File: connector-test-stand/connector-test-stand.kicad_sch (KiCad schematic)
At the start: 85 parts, among them J1 Conn_01x02, J10 Conn_01x04_MountingPin, J11 DE9_Socket_MountingHoles, J12 DVI-I_Dual_Link, J2 Conn_01x02, J3 Conn_01x02, J4 Conn_01x05, J5 Conn_01x04_MountingPin, J6 Conn_01x02, J7 Conn_01x03, J8 Conn_01x10, J9 Conn_01x04_MountingPin, K1 G2RL-1-E, U1 PCF8574RGTR, U10 SN65HVD11HD, U11 74AHCT1G04, U12 CDSOT236-0504C, U13 MCP1501-40xSN, U2 INA333xxDGK, U4 74LS540, U5 OPA333xxD, U6 SN74LVC1G125DBV, U7 TBD62783A, U8 SN74LVC1G125DBV, U9 P82B96

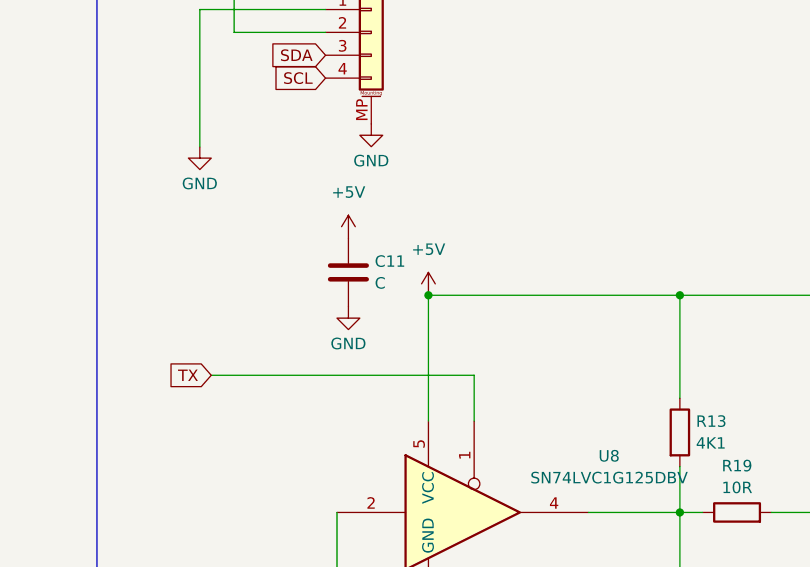
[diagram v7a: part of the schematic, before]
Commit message: Update missing component values
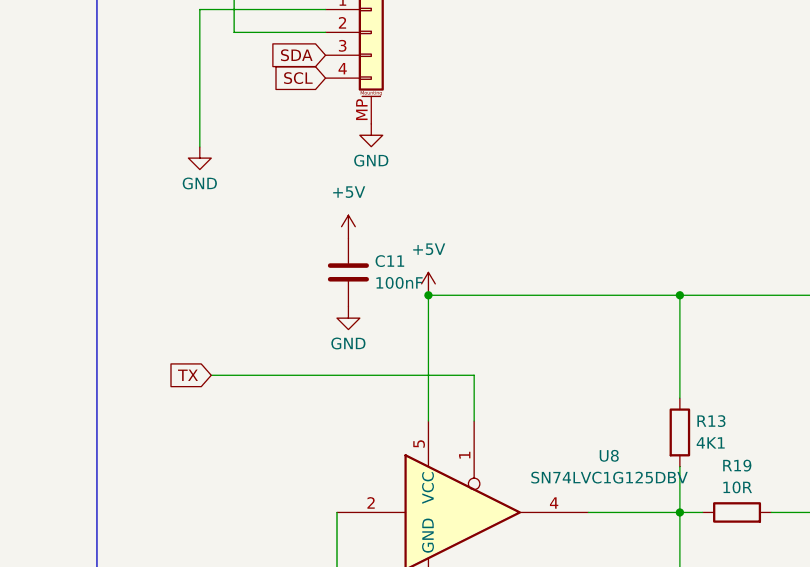
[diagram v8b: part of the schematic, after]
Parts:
- C11: value C -> 100nF
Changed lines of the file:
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@@
 			)
 		)
-		(property "Value" "C"
+		(property "Value" "100nF"
 			(at 236.601 97.7321 0)
 			(effects
